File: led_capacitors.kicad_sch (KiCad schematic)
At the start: 90 parts

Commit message: added footprints to compontents
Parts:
- C1, C10, C11, C12, C13, C14, C15, C16, C17, C18, C19, C2, C20, C21, C22, C23, C24, C25, C26, C27, C28, C29, C3, C30, C31, C32, C33, C34, C35, C36, C37, C38, C39, C4, C40, C41, C42, C43, C44, C45, C46, C47, C48, C49, C5, C50, C51, C52, C53, C54, C55, C56, C57, C58, C59, C6, C60, C61, C62, C63, C64, C65, C66, C67, C68, C69, C7, C70, C71, C72, C73, C74, C75, C76, C77, C78, C79, C8, C80, C81, C82, C83, C84, C85, C86, C87, C88, C89, C9, C90: footprint (none) -> Capacitor_SMD:C_0402_1005Metric

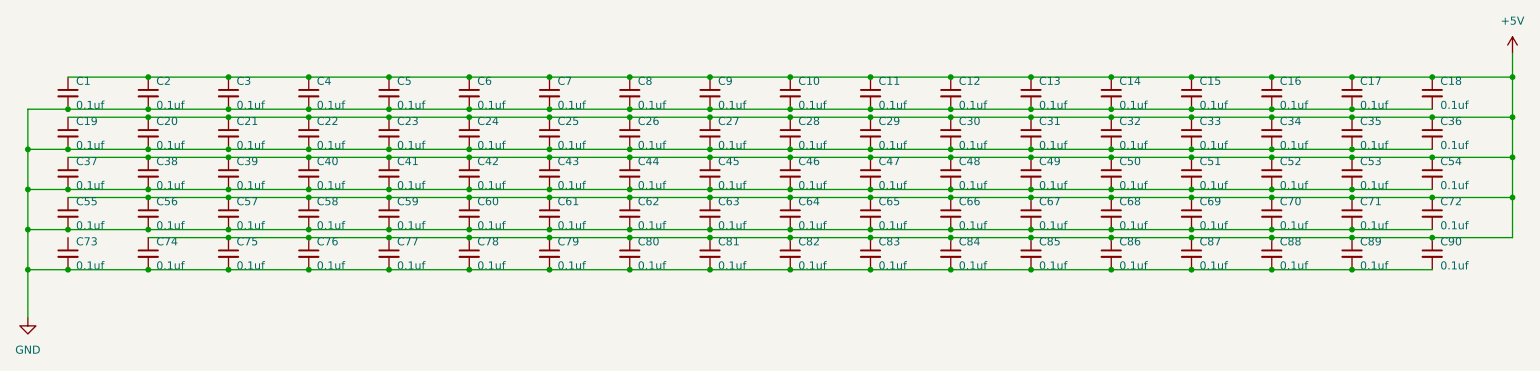
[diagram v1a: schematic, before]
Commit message: placed switches and LEDs
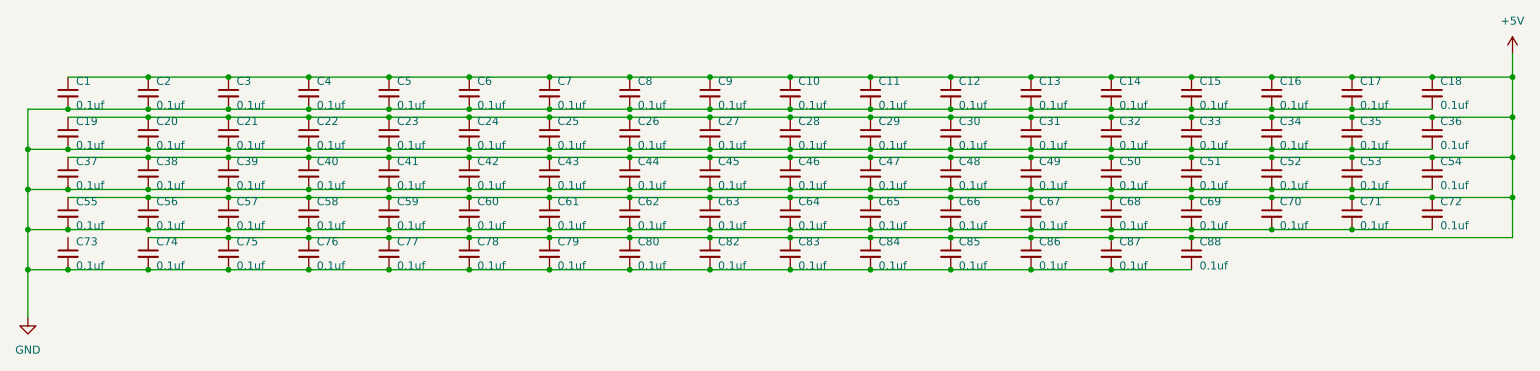
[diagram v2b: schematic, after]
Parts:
- removed C88, C89, C90: 0.1uf, Capacitor_SMD:C_0402_1005Metric, symbol Device:C_Small
- renumbered C81 to C82, C82 to C83, C83 to C84, C84 to C85, C85 to C86, C86 to C87, C87 to C88
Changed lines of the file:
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@@
   (junction (at 76.2 49.53) (diameter 0) (color 0 0 0 0)
   )
-  (junction (at 215.9 55.88) (diameter 0) (color 0 0 0 0)
-  )
   (junction (at 165.1 36.83) (diameter 0) (color 0 0 0 0)
   )
@@
   (junction (at 228.6 38.1) (diameter 0) (color 0 0 0 0)
   )
-  (junction (at 228.6 50.8) (diameter 0) (color 0 0 0 0)
-  )
   (junction (at 165.1 49.53) (diameter 0) (color 0 0 0 0)
   )
@@
   (junction (at 38.1 38.1) (diameter 0) (color 0 0 0 0)
   )
-  (junction (at 215.9 50.8) (diameter 0) (color 0 0 0 0)
-  )
   (junction (at 127 31.75) (diameter 0) (color 0 0 0 0)
   )
@@
   (junction (at 88.9 43.18) (diameter 0) (color 0 0 0 0)
   )
-  (junction (at 241.3 50.8) (diameter 0) (color 0 0 0 0)
-  )
   (junction (at 228.6 43.18) (diameter 0) (color 0 0 0 0)
   )
@@
   (junction (at 165.1 55.88) (diameter 0) (color 0 0 0 0)
   )
-  (junction (at 228.6 55.88) (diameter 0) (color 0 0 0 0)
-  )
   (junction (at 76.2 43.18) (diameter 0) (color 0 0 0 0)
   )
@@
   (junction (at 152.4 38.1) (diameter 0) (color 0 0 0 0)
   )
-  (junction (at 203.2 55.88) (diameter 0) (color 0 0 0 0)
-  )
   (junction (at 25.4 55.88) (diameter 0) (color 0 0 0 0)
   )
@@
     (stroke (width 0) (type default) (color 0 0 0 0))
   )
-  (wire (pts (xy 228.6 50.8) (xy 241.3 50.8))
-    (stroke (width 0) (type default) (color 0 0 0 0))
-  )
   (wire (pts (xy 177.8 43.18) (xy 165.1 43.18))
     (stroke (width 0) (type default) (color 0 0 0 0))
@@
     (stroke (width 0) (type default) (color 0 0 0 0))
   )
-  (wire (pts (xy 215.9 50.8) (xy 228.6 50.8))
-    (stroke (width 0) (type default) (color 0 0 0 0))
-  )
   (wire (pts (xy 165.1 55.88) (xy 152.4 55.88))
     (stroke (width 0) (type default) (color 0 0 0 0))
@@
     (stroke (width 0) (type default) (color 0 0 0 0))
   )
-  (wire (pts (xy 215.9 55.88) (xy 203.2 55.88))
-    (stroke (width 0) (type default) (color 0 0 0 0))
-  )
   (wire (pts (xy 228.6 38.1) (xy 241.3 38.1))
     (stroke (width 0) (type default) (color 0 0 0 0))
@@
     (stroke (width 0) (type default) (color 0 0 0 0))
   )
-  (wire (pts (xy 241.3 50.8) (xy 254 50.8))
+  (wire (pts (xy 203.2 50.8) (xy 254 50.8))
     (stroke (width 0) (type default) (color 0 0 0 0))
   )
@@
     (stroke (width 0) (type default) (color 0 0 0 0))
   )
-  (wire (pts (xy 228.6 55.88) (xy 215.9 55.88))
-    (stroke (width 0) (type default) (color 0 0 0 0))
-  )
   (wire (pts (xy 25.4 25.4) (xy 38.1 25.4))
     (stroke (width 0) (type default) (color 0 0 0 0))
@@
     (stroke (width 0) (type default) (color 0 0 0 0))
   )
-  (wire (pts (xy 241.3 55.88) (xy 228.6 55.88))
-    (stroke (width 0) (type default) (color 0 0 0 0))
-  )
   (wire (pts (xy 127 49.53) (xy 114.3 49.53))
     (stroke (width 0) (type default) (color 0 0 0 0))
@@
     (stroke (width 0) (type default) (color 0 0 0 0))
   )
-  (wire (pts (xy 203.2 50.8) (xy 215.9 50.8))
-    (stroke (width 0) (type default) (color 0 0 0 0))
-  )
   (wire (pts (xy 203.2 49.53) (xy 190.5 49.53))
     (stroke (width 0) (type default) (color 0 0 0 0))
@@
     (pin "2")
   )
-  (symbol (lib_id "Device:C_Small") (at 215.9 53.34 0) (unit 1)
-    (in_bom yes) (on_board yes)
-    (property "Reference" "C88" (id 0) (at 217.17 51.435 0)
-      (effects (font (size 1.27 1.27)) (justify left))
-    )
-    (property "Value" "0.1uf" (id 1) (at 217.17 55.245 0)
-      (effects (font (size 1.27 1.27)) (justify left))
-    )
-    (property "Footprint" "Capacitor_SMD:C_0402_1005Metric" (id 2) (at 215.9 53.34 0)
-      (effects (font (size 1.27 1.27)) hide)
-    )
-    (property "Datasheet" "~" (id 3) (at 215.9 53.34 0)
-      (effects (font (size 1.27 1.27)) hide)
-    )
-    (pin "1")
-    (pin "2")
-  )
   (symbol (lib_id "Device:C_Small") (at 114.3 40.64 0) (unit 1)
     (in_bom yes) (on_board yes)
@@
     (pin "2")
   )
-  (symbol (lib_id "Device:C_Small") (at 241.3 53.34 0) (unit 1)
-    (in_bom yes) (on_board yes)
-    (property "Reference" "C90" (id 0) (at 242.57 51.435 0)
-      (effects (font (size 1.27 1.27)) (justify left))
-    )
-    (property "Value" "0.1uf" (id 1) (at 242.57 55.245 0)
-      (effects (font (size 1.27 1.27)) (justify left))
-    )
-    (property "Footprint" "Capacitor_SMD:C_0402_1005Metric" (id 2) (at 241.3 53.34 0)
-      (effects (font (size 1.27 1.27)) hide)
-    )
-    (property "Datasheet" "~" (id 3) (at 241.3 53.34 0)
-      (effects (font (size 1.27 1.27)) hide)
-    )
-    (pin "1")
-    (pin "2")
-  )
   (symbol (lib_id "Device:C_Small") (at 76.2 40.64 0) (unit 1)
     (in_bom yes) (on_board yes)
@@
   (symbol (lib_id "Device:C_Small") (at 152.4 53.34 0) (unit 1)
     (in_bom yes) (on_board yes)
-    (property "Reference" "C83" (id 0) (at 153.67 51.435 0)
+    (property "Reference" "C84" (id 0) (at 153.67 51.435 0)
       (effects (font (size 1.27 1.27)) (justify left))
     )
@@
   (symbol (lib_id "Device:C_Small") (at 127 53.34 0) (unit 1)
     (in_bom yes) (on_board yes)
-    (property "Reference" "C81" (id 0) (at 128.27 51.435 0)
+    (property "Reference" "C82" (id 0) (at 128.27 51.435 0)
       (effects (font (size 1.27 1.27)) (justify left))
     )
@@
   (symbol (lib_id "Device:C_Small") (at 139.7 53.34 0) (unit 1)
     (in_bom yes) (on_board yes)
-    (property "Reference" "C82" (id 0) (at 140.97 51.435 0)
+    (property "Reference" "C83" (id 0) (at 140.97 51.435 0)
       (effects (font (size 1.27 1.27)) (justify left))
     )
@@
   (symbol (lib_id "Device:C_Small") (at 165.1 53.34 0) (unit 1)
     (in_bom yes) (on_board yes)
-    (property "Reference" "C84" (id 0) (at 166.37 51.435 0)
+    (property "Reference" "C85" (id 0) (at 166.37 51.435 0)
       (effects (font (size 1.27 1.27)) (justify left))
     )
@@
   (symbol (lib_id "Device:C_Small") (at 177.8 53.34 0) (unit 1)
     (in_bom yes) (on_board yes)
-    (property "Reference" "C85" (id 0) (at 179.07 51.435 0)
+    (property "Reference" "C86" (id 0) (at 179.07 51.435 0)
       (effects (font (size 1.27 1.27)) (justify left))
     )
@@
   (symbol (lib_id "Device:C_Small") (at 203.2 53.34 0) (unit 1)
     (in_bom yes) (on_board yes)
-    (property "Reference" "C87" (id 0) (at 204.47 51.435 0)
+    (property "Reference" "C88" (id 0) (at 204.47 51.435 0)
       (effects (font (size 1.27 1.27)) (justify left))
     )
@@
   (symbol (lib_id "Device:C_Small") (at 190.5 53.34 0) (unit 1)
     (in_bom yes) (on_board yes)
-    (property "Reference" "C86" (id 0) (at 191.77 51.435 0)
+    (property "Reference" "C87" (id 0) (at 191.77 51.435 0)
       (effects (font (size 1.27 1.27)) (justify left))
     )
@@
       (effects (font (size 1.27 1.27)) hide)
     )
-    (pin "1")
-    (pin "2")
-  )
-  (symbol (lib_id "Device:C_Small") (at 228.6 53.34 0) (unit 1)
-    (in_bom yes) (on_board yes)
-    (property "Reference" "C89" (id 0) (at 229.87 51.435 0)
-      (effects (font (size 1.27 1.27)) (justify left))
-    )
-    (property "Value" "0.1uf" (id 1) (at 229.87 55.245 0)
-      (effects (font (size 1.27 1.27)) (justify left))
-    )
-    (property "Footprint" "Capacitor_SMD:C_0402_1005Metric" (id 2) (at 228.6 53.34 0)
-      (effects (font (size 1.27 1.27)) hide)
-    )
-    (property "Datasheet" "~" (id 3) (at 228.6 53.34 0)
-      (effects (font (size 1.27 1.27)) hide)
-    )
